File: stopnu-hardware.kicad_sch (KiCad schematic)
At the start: 17 parts, among them CN1 SM04B-SRSS-TB (LF)(SN), CN2 OQ0232510000G, CN3 OQ0232510000G, CN4 OQ0232510000G, CN5 OQ0232510000G, CN6 OQ0432510000G, J1 Conn_02x15_Odd_Even

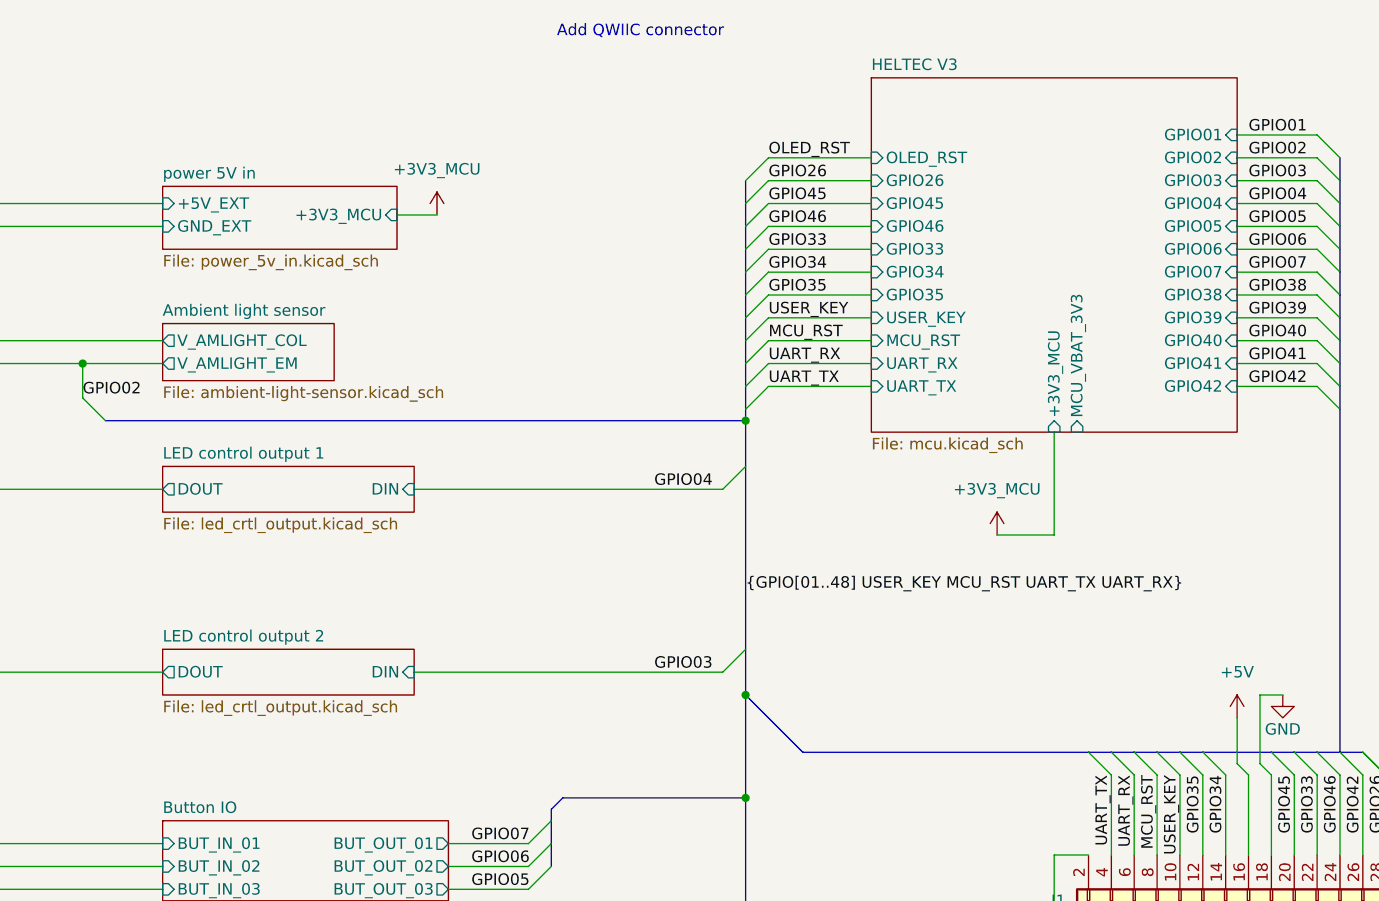
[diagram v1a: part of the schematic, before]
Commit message: Add README.md, make power input more intuitive in schematic.
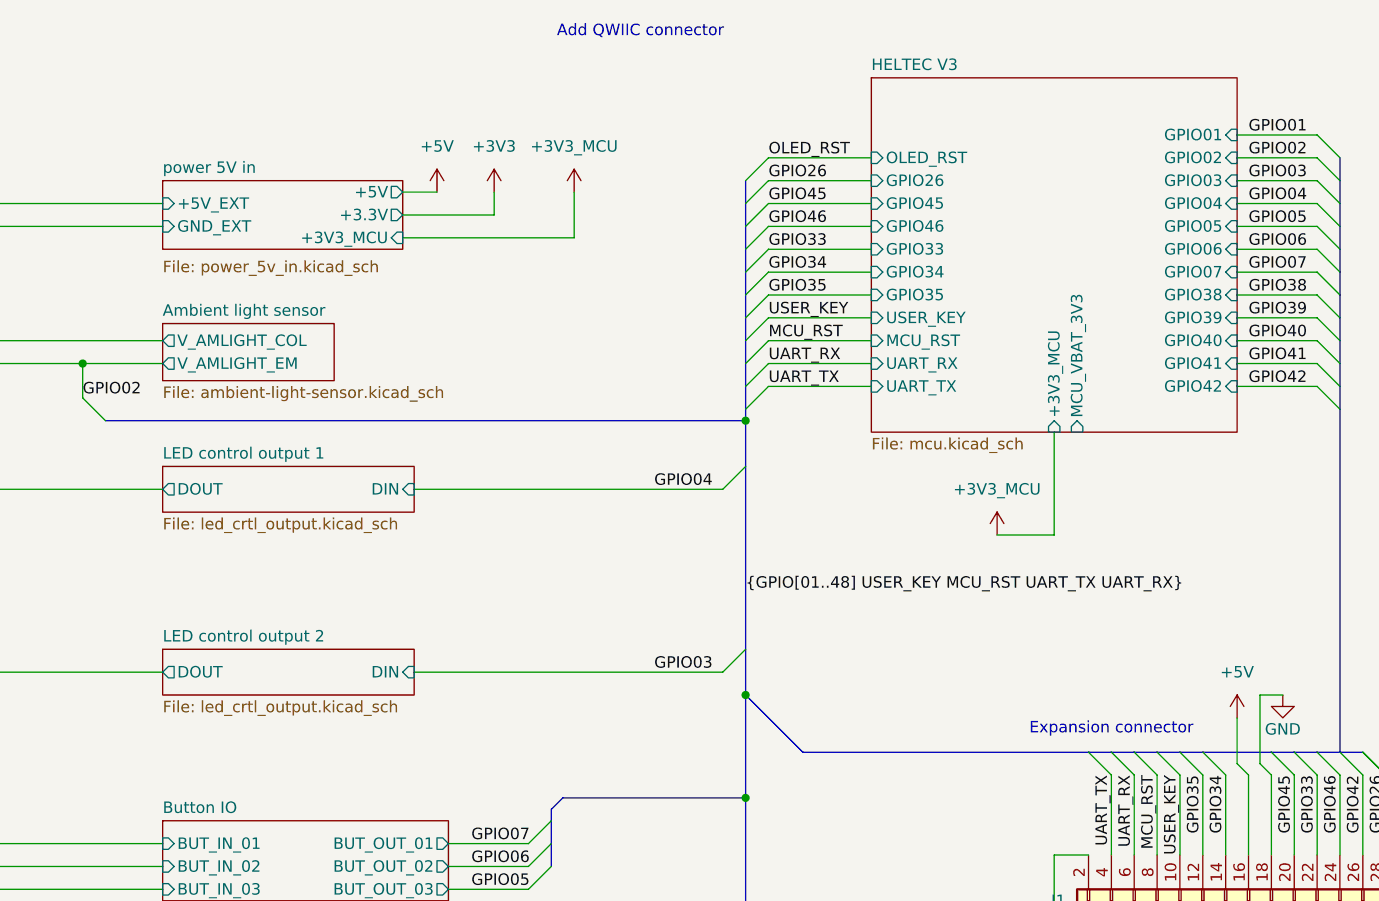
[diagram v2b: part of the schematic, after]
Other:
- sheet power 5V in ports: added +3.3V, +5V; removed none
- note added: "Expansion connector"
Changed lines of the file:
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@@
 		)
 	)
+	(text "Expansion connector"
+		(exclude_from_sim no)
+		(at 182.88 97.79 0)
+		(effects
+			(font
+				(size 1.27 1.27)
+			)
+		)
+	)
 	(junction
 		(at 55.88 149.86)
@@
 	(wire
 		(pts
+			(xy 114.3 38.1) (xy 114.3 40.64)
+		)
+		(stroke
+			(width 0)
+			(type default)
+		)
+	)
+	(wire
+		(pts
 			(xy 30.48 144.78) (xy 40.64 144.78)
 		)
@@
 	(wire
 		(pts
+			(xy 104.14 38.1) (xy 107.95 38.1)
+		)
+		(stroke
+			(width 0)
+			(type default)
+		)
+	)
+	(wire
+		(pts
 			(xy 195.58 102.87) (xy 195.58 111.76)
 		)
@@
 		)
 	)
+	(wire
+		(pts
+			(xy 123.19 43.18) (xy 123.19 38.1)
+		)
+		(stroke
+			(width 0)
+			(type default)
+		)
+	)
 	(bus
 		(pts
@@
 	(wire
 		(pts
-			(xy 33.02 57.15) (xy 68.58 57.15)
+			(xy 104.14 40.64) (xy 114.3 40.64)
 		)
 		(stroke
@@
 	(wire
 		(pts
-			(xy 199.39 93.98) (xy 201.93 93.98)
+			(xy 33.02 57.15) (xy 68.58 57.15)
 		)
 		(stroke
@@
 		)
 	)
-	(bus
+	(wire
 		(pts
-			(xy 208.28 44.45) (xy 208.28 46.99)
+			(xy 199.39 93.98) (xy 201.93 93.98)
 		)
 		(stroke
@@
 		)
 	)
-	(wire
+	(bus
 		(pts
-			(xy 219.71 111.76) (xy 215.9 111.76)
+			(xy 208.28 44.45) (xy 208.28 46.99)
 		)
 		(stroke
@@
 	(wire
 		(pts
-			(xy 68.58 57.15) (xy 68.58 60.96)
+			(xy 219.71 111.76) (xy 215.9 111.76)
 		)
 		(stroke
@@
 	(wire
 		(pts
-			(xy 103.505 40.64) (xy 107.95 40.64)
+			(xy 68.58 57.15) (xy 68.58 60.96)
 		)
 		(stroke
@@
 		)
 	)
+	(wire
+		(pts
+			(xy 104.14 43.18) (xy 123.19 43.18)
+		)
+		(stroke
+			(width 0)
+			(type default)
+		)
+	)
 	(bus
 		(pts
@@
 	(symbol
 		(lib_id "power:+3V3")
-		(at 107.95 40.64 0)
+		(at 123.19 38.1 0)
 		(unit 1)
 		(exclude_from_sim no)
@@
 		(fields_autoplaced yes)
 		(property "Reference" "#PWR011"
-			(at 107.95 44.45 0)
+			(at 123.19 41.91 0)
 			(effects
 				(font
@@
 		)
 		(property "Value" "+3V3_MCU"
-			(at 107.95 35.56 0)
+			(at 123.19 33.02 0)
 			(effects
 				(font
@@
 		)
 		(property "Footprint" ""
-			(at 107.95 40.64 0)
+			(at 123.19 38.1 0)
 			(effects
 				(font
@@
 		)
 		(property "Datasheet" ""
-			(at 107.95 40.64 0)
+			(at 123.19 38.1 0)
 			(effects
 				(font
@@
 		)
 		(property "Description" "Power symbol creates a global label with name \"+3V3\""
-			(at 107.95 40.64 0)
+			(at 123.19 38.1 0)
 			(effects
 				(font
@@
 	)
 	(symbol
+		(lib_id "power:+3V3")
+		(at 114.3 38.1 0)
+		(unit 1)
+		(exclude_from_sim no)
+		(in_bom yes)
+		(on_board yes)
+		(dnp no)
+		(fields_autoplaced yes)
+		(property "Reference" "#PWR041"
+			(at 114.3 41.91 0)
+			(effects
+				(font
+					(size 1.27 1.27)
+				)
+				(hide yes)
+			)
+		)
+		(property "Value" "+3V3"
+			(at 114.3 33.02 0)
+			(effects
+				(font
+					(size 1.27 1.27)
+				)
+			)
+		)
+		(property "Footprint" ""
+			(at 114.3 38.1 0)
+			(effects
+				(font
+					(size 1.27 1.27)
+				)
+				(hide yes)
+			)
+		)
+		(property "Datasheet" ""
+			(at 114.3 38.1 0)
+			(effects
+				(font
+					(size 1.27 1.27)
+				)
+				(hide yes)
+			)
+		)
+		(property "Description" "Power symbol creates a global label with name \"+3V3\""
+			(at 114.3 38.1 0)
+			(effects
+				(font
+					(size 1.27 1.27)
+				)
+				(hide yes)
+			)
+		)
+		(pin "1"
+		)
+		(instances
+			(project ""
+				(path "/4ab90003-ea4c-4878-8117-f834ac24f8d9"
+					(reference "#PWR041")
+					(unit 1)
+				)
+			)
+		)
+	)
+	(symbol
 		(lib_id "Mechanical:MountingHole_Pad")
 		(at 39.37 177.8 0)
@@
 	)
 	(symbol
+		(lib_id "power:+5V")
+		(at 107.95 38.1 0)
+		(unit 1)
+		(exclude_from_sim no)
+		(in_bom yes)
+		(on_board yes)
+		(dnp no)
+		(fields_autoplaced yes)
+		(property "Reference" "#PWR036"
+			(at 107.95 41.91 0)
+			(effects
+				(font
+					(size 1.27 1.27)
+				)
+				(hide yes)
+			)
+		)
+		(property "Value" "+5V"
+			(at 107.95 33.02 0)
+			(effects
+				(font
+					(size 1.27 1.27)
+				)
+			)
+		)
+		(property "Footprint" ""
+			(at 107.95 38.1 0)
+			(effects
+				(font
+					(size 1.27 1.27)
+				)
+				(hide yes)
+			)
+		)
+		(property "Datasheet" ""
+			(at 107.95 38.1 0)
+			(effects
+				(font
+					(size 1.27 1.27)
+				)
+				(hide yes)
+			)
+		)
+		(property "Description" "Power symbol creates a global label with name \"+5V\""
+			(at 107.95 38.1 0)
+			(effects
+				(font
+					(size 1.27 1.27)
+				)
+				(hide yes)
+			)
+		)
+		(pin "1"
+		)
+		(instances
+			(project ""
+				(path "/4ab90003-ea4c-4878-8117-f834ac24f8d9"
+					(reference "#PWR036")
+					(unit 1)
+				)
+			)
+		)
+	)
+	(symbol
 		(lib_id "lcsc:SM04B-SRSS-TB(LF)(SN)")
 		(at 26.67 148.59 270)
@@
 	)
 	(sheet
-		(at 77.47 37.465)
-		(size 26.035 6.985)
+		(at 77.47 36.83)
+		(size 26.67 7.62)
 		(exclude_from_sim no)
 		(in_bom yes)
@@
 		)
 		(property "Sheetname" "power 5V in"
-			(at 77.47 36.7534 0)
+			(at 77.47 36.1184 0)
 			(effects
 				(font
@@
 		)
 		(property "Sheetfile" "power_5v_in.kicad_sch"
-			(at 77.47 45.0346 0)
+			(at 77.47 45.6696 0)
 			(effects
 				(font
@@
 		)
 		(pin "+3V3_MCU" input
-			(at 103.505 40.64 0)
+			(at 104.14 43.18 0)
+			(effects
+				(font
+					(size 1.27 1.27)
+				)
+				(justify right)
+			)
+		)
+		(pin "+3.3V" output
+			(at 104.14 40.64 0)
+			(effects
+				(font
+					(size 1.27 1.27)
+				)
+				(justify right)
+			)
+		)
+		(pin "+5V" output
+			(at 104.14 38.1 0)
 			(effects
 				(font

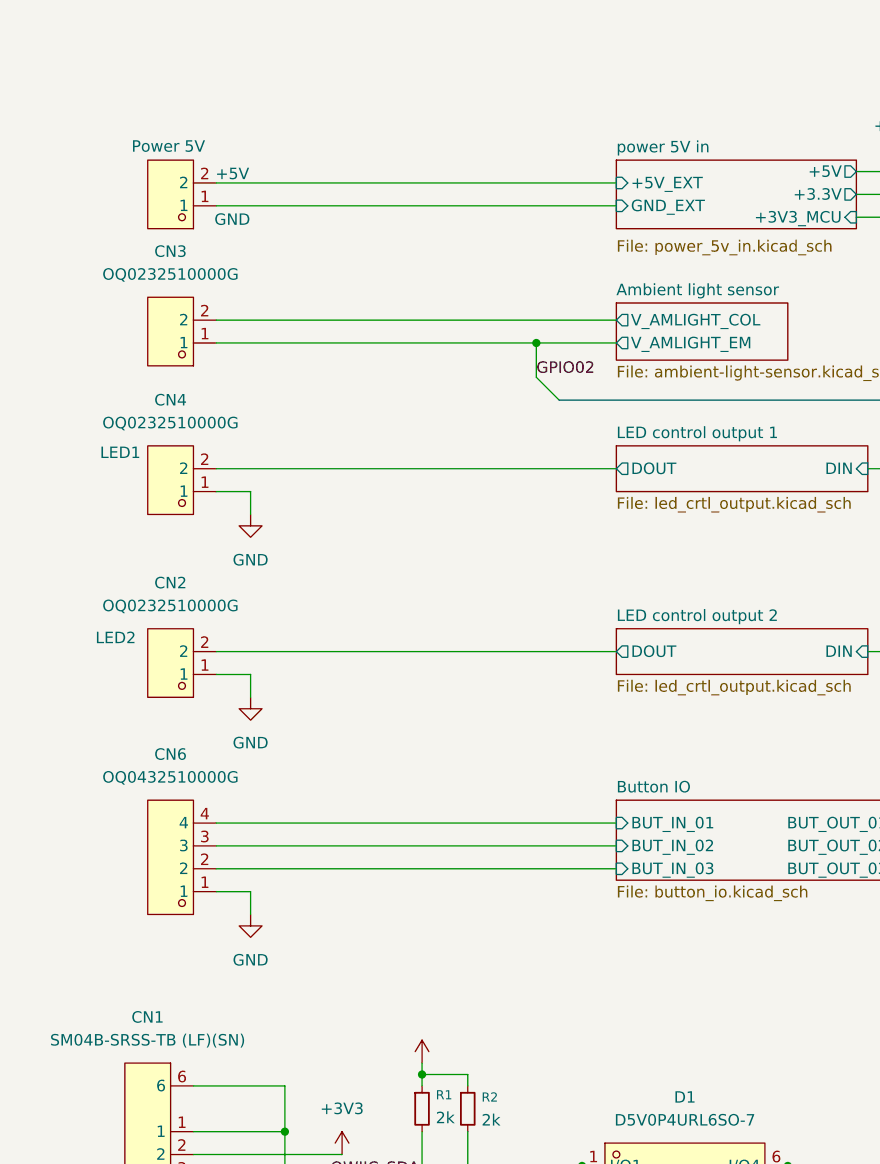
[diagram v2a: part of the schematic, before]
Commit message: Fixed issues + added 3 2 pin connectors for digital (button) inputs.
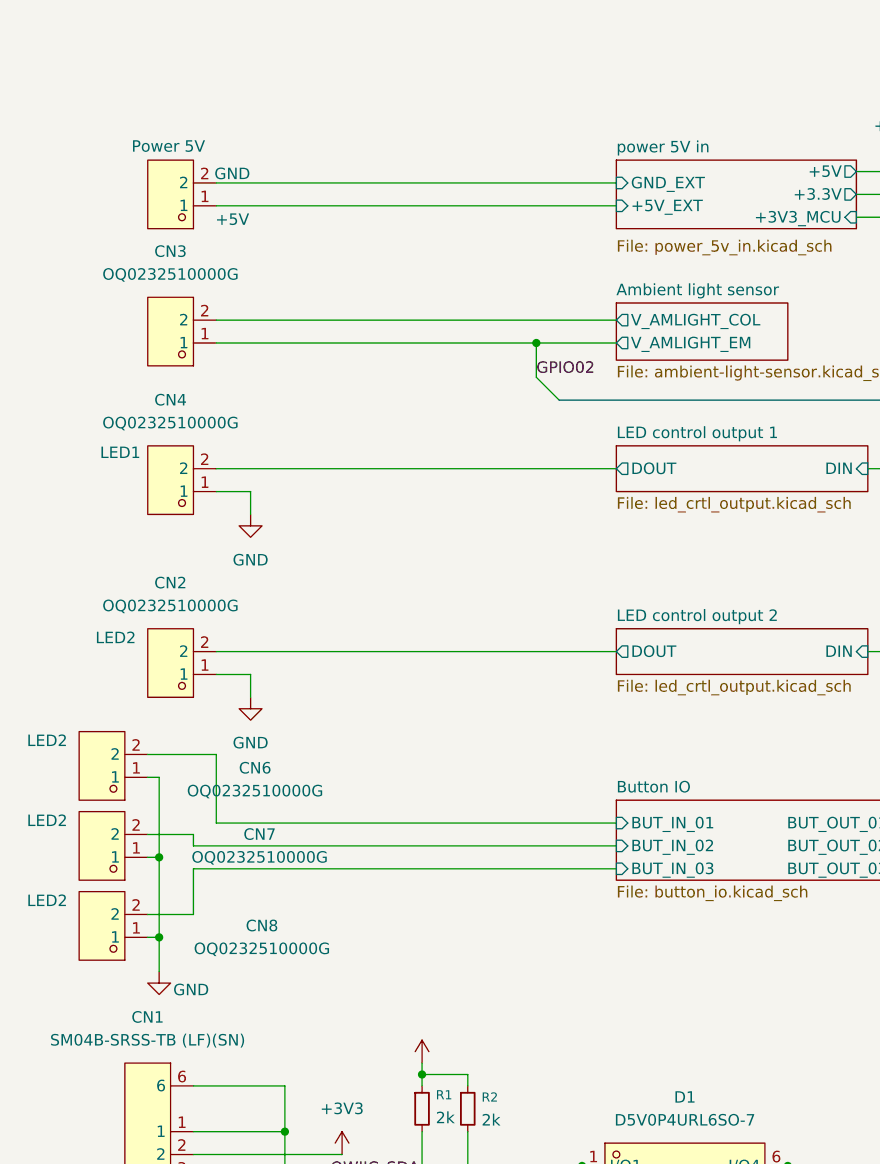
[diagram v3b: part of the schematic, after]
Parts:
- removed CN6: OQ0432510000G, lcsc:CONN-TH_4P-P3.81_OQ0432510000G, symbol lcsc:OQ0432510000G
- added CN6, CN7, CN8: OQ0232510000G, lcsc:CONN-TH_OQ0232510000G, symbol lcsc:OQ0232510000G
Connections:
- net Button IO/BUT_IN_01: now also CN6.2
- net Button IO/BUT_IN_02: now also CN7.2
- net Button IO/BUT_IN_03: now also CN8.2
- net GND: now also CN6.1, CN7.1, CN8.1
- net power 5V in/+5V_EXT: now also CN5.1; no longer CN5.2
- net power 5V in/GND_EXT: now also CN5.2; no longer CN5.1

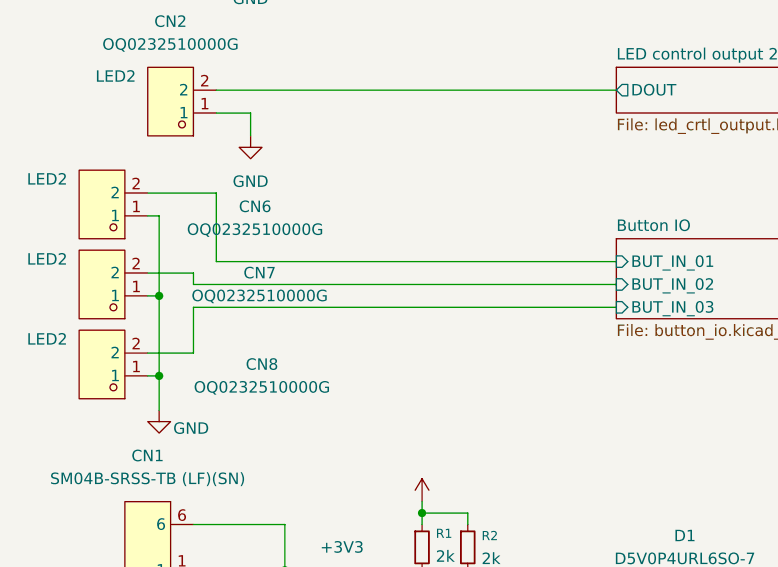
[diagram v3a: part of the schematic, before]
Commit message: Fixed labels 3 digital input channels.
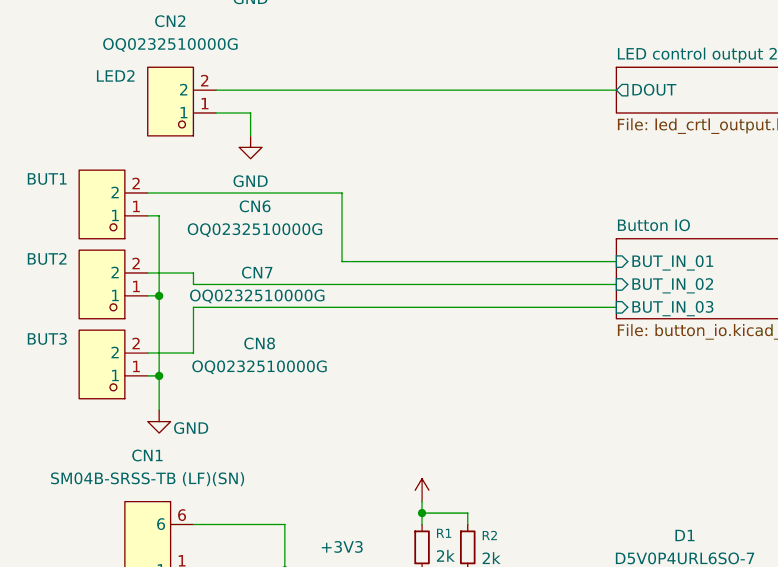
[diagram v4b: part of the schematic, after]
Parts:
- CN6: Label2 LED2 -> BUT1; S S -> S-1
- CN7: Label2 LED2 -> BUT2; S S -> S-2
- CN8: Label2 LED2 -> BUT3; S S -> S-3
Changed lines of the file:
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@@
 	(wire
 		(pts
-			(xy 25.4 102.87) (xy 33.02 102.87)
+			(xy 25.4 102.87) (xy 46.99 102.87)
 		)
 		(stroke
@@
 	(wire
 		(pts
-			(xy 33.02 102.87) (xy 33.02 110.49)
+			(xy 46.99 102.87) (xy 46.99 110.49)
 		)
 		(stroke
@@
 	(wire
 		(pts
-			(xy 33.02 110.49) (xy 77.47 110.49)
+			(xy 46.99 110.49) (xy 77.47 110.49)
 		)
 		(stroke
@@
 			)
 		)
-		(property "Label2" "LED2"
+		(property "Label2" "BUT1"
 			(at 14.224 101.346 0)
 			(effects
@@
 			)
 		)
-		(property "S" "S"
+		(property "S" "S-1"
 			(at 20.32 104.14 0)
 			(effects
@@
 		(dnp no)
 		(property "Reference" "CN8"
-			(at 38.1 121.92 0)
+			(at 37.846 119.634 0)
 			(effects
 				(font
@@
 		)
 		(property "Value" "OQ0232510000G"
-			(at 38.1 124.46 0)
+			(at 37.846 122.174 0)
 			(effects
 				(font
@@
 			)
 		)
-		(property "Label2" "LED2"
+		(property "Label2" "BUT3"
 			(at 14.224 119.126 0)
 			(effects
@@
 			)
 		)
-		(property "S" "S"
+		(property "S" "S-3"
 			(at 20.32 121.92 0)
 			(effects
@@
 		(dnp no)
 		(property "Reference" "CN7"
-			(at 37.846 111.76 0)
+			(at 37.592 111.76 0)
 			(effects
 				(font
@@
 		)
 		(property "Value" "OQ0232510000G"
-			(at 37.846 114.3 0)
+			(at 37.592 114.3 0)
 			(effects
 				(font
@@
 			)
 		)
-		(property "Label2" "LED2"
+		(property "Label2" "BUT2"
 			(at 14.224 110.236 0)
 			(effects
@@
 			)
 		)
-		(property "S" "S"
+		(property "S" "S-2"
 			(at 20.32 113.03 0)
 			(effects
